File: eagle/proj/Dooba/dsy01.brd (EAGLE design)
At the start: 100 x 80 mm, 73 parts, among them U1 STM32F071LQFP100, U10 S25FLXXXSSOIC16, U2 AS6C1608TSOPII-44, U3 STM32F030LQFP32, U4 STM32F030LQFP32, U5 STM32F030LQFP32, U6 STM32F030LQFP32, U7 STM32F030LQFP32, U8 MIC550XSOT23, U9 STM32F030LQFP32, X1 8MHz, X2 8MHz, X3 8MHz, X4 8MHz, X5 8MHz, X6 8MHz, X7 8MHz

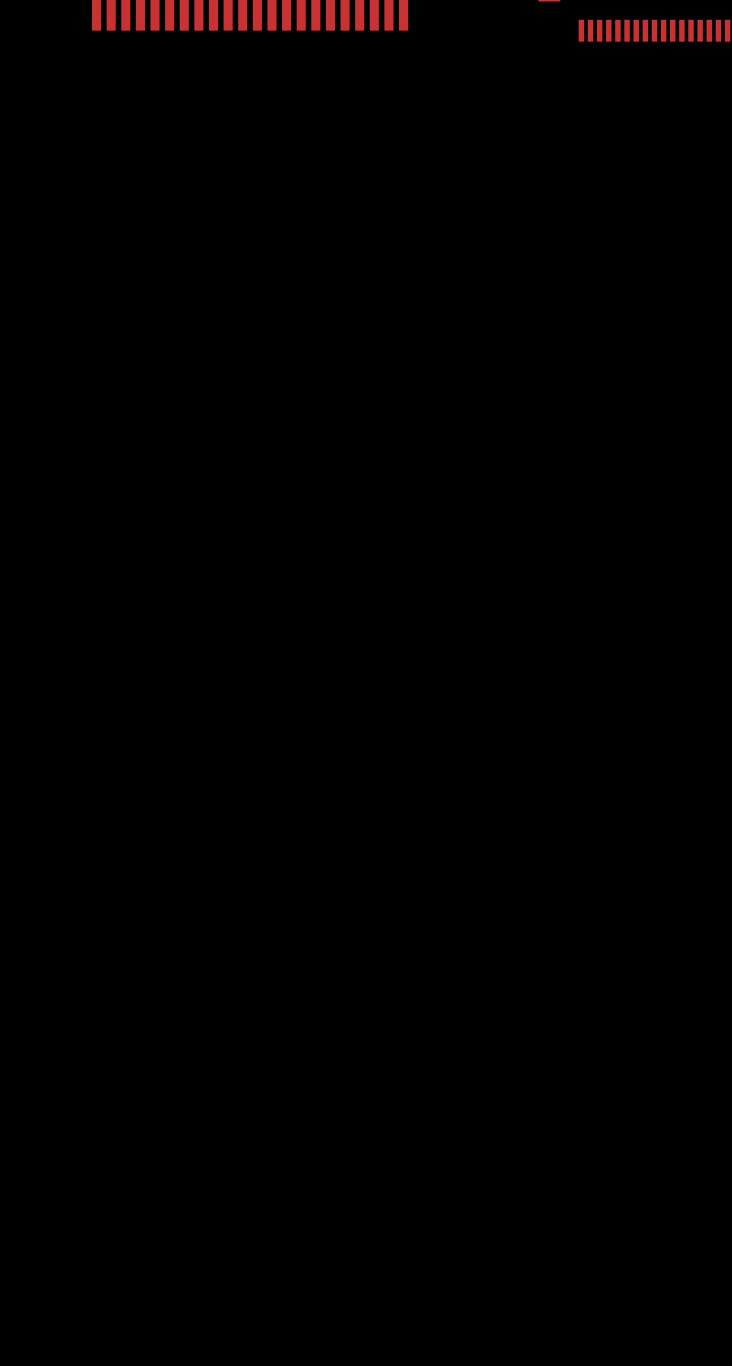
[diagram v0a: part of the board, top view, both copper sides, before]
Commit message: Added more Pin headers to Dooba Eagle Lib Added RST signal and extension header to DSY01
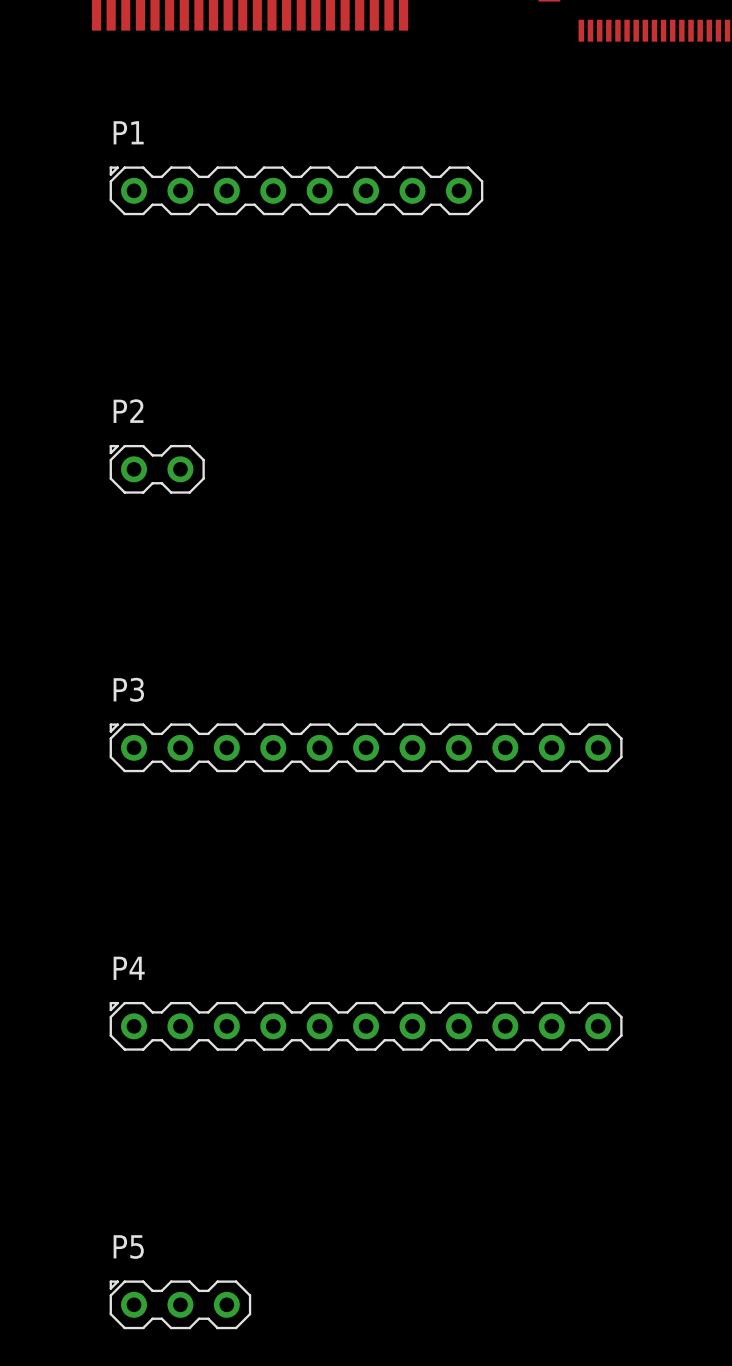
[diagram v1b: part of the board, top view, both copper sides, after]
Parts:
- added P1: DIO, dooba:PIN_8
- added P2: CKI-CKO, dooba:PIN_2
- added P3: NOT, dooba:PIN_11
- added P4: RDY, dooba:PIN_11
- added P5: PWR(VIN-GND-RST), dooba:PIN_3
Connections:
- new net N$35: P5.3, U1.14, U3.4, U5.4, U6.4, U7.4, U9.4
- new net N$36: U1.1, U2.41
- new net N$37: U1.2, U2.17
- new net N$38: U1.3, U2.40
- new net N$39: U1.4, U2.6
- net GND: now also P5.2
- net N$34: now also P5.1
- net N$55: now also P1.2
- net N$57: now also P3.5
- net N$58: now also P3.4
- net N$59: now also P3.3
- net N$60: now also P3.2
- net N$61: now also P3.1
- net N$63: now also P1.3
- net N$64: now also P3.6
- net N$65: now also P3.7
- net N$66: now also P3.8
- net N$67: now also P3.9
- net N$68: now also P3.10
- net N$69: now also P3.11
- net N$71: now also P1.4
- net N$72: now also P1.5
- net N$73: now also P1.6
- net N$75: now also P4.1
- net N$76: now also P4.2
- net N$77: now also P4.3
- net N$78: now also P4.4
- net N$79: now also P4.5
- net N$80: now also P4.8
- net N$81: now also P4.7
- net N$82: now also P4.6
- net N$83: now also P4.9
- net N$84: now also P4.10
- net N$85: now also P4.11
- net N$93: now also P1.7
- net N$94: now also P1.8
- net N$95: now also P2.2
- net N$96: now also P2.1
- net N$97: now also P1.1

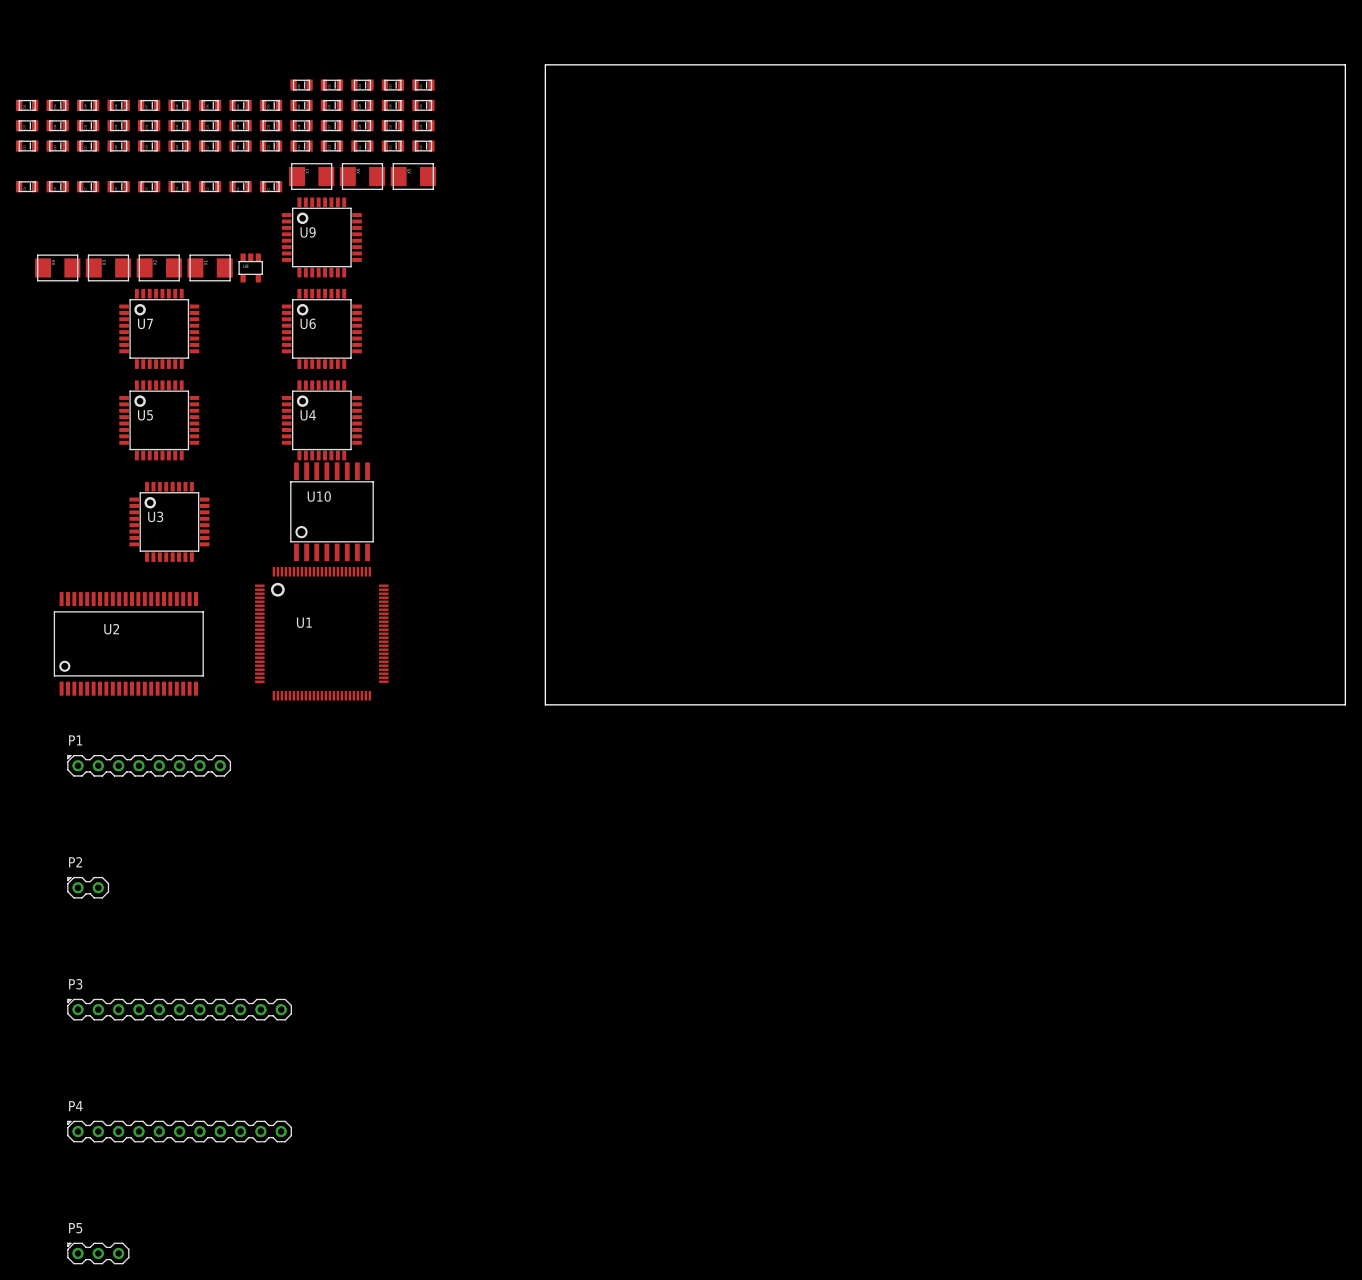
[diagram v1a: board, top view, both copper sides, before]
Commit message: Added CAM and DRU files for Eagle Further routed DSY01 board
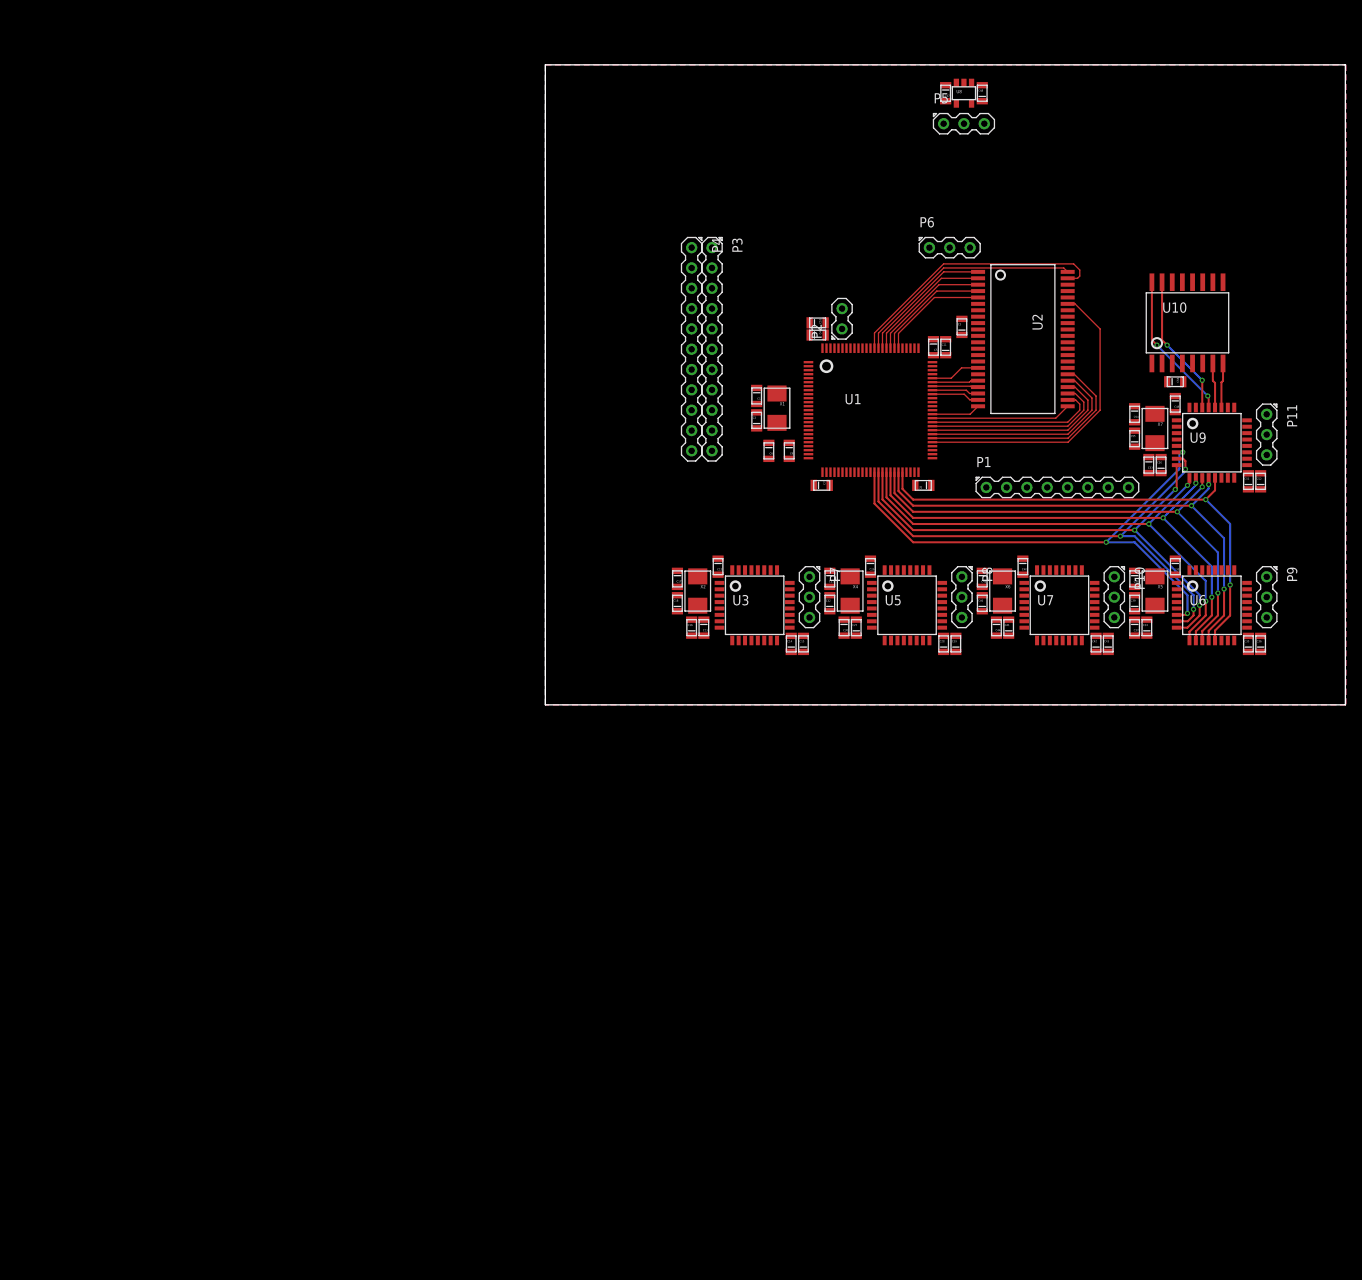
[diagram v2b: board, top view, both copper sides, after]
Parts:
- removed C19, C21: 100nF, dooba:0805
- removed C20: 10nF, dooba:0805
- removed C22: 4.7uF, dooba:0805
- removed C23: 1uF, dooba:0805
- removed C24, C25: 27pF, dooba:0805
- removed U4: STM32F030LQFP32, dooba:QFP32
- removed X3: 8MHz, dooba:XTAL_532
- added P10, P11, P6, P7, P8, P9: SWD_CORE(SWCLK-SWDIO-GND), dooba:PIN_3
- moved P5 177.9 mm to (52.3, 72.6)
- moved C36 163.7 mm to (89.4, 7.62), turned to 270 degrees
- moved C51 159.7 mm to (87.9, 27.9), turned to 270 degrees
- moved C35 158.8 mm to (87.9, 7.62), turned to 270 degrees
- moved C37 152.0 mm to (73.7, 9.65), turned to 90 degrees
- moved C50 145.1 mm to (77.0, 30.0), turned to 270 degrees
- moved C34 143.0 mm to (75.2, 9.65), turned to 270 degrees
- moved C49 140.9 mm to (78.7, 37.6), turned to 90 degrees
- moved C33 139.6 mm to (78.7, 17.3), turned to 90 degrees
- moved C43 124.4 mm to (70.4, 7.62), turned to 270 degrees
- moved C42 120.0 mm to (68.8, 7.62), turned to 270 degrees
- moved P1 118.8 mm to (64.0, 27.2)
- moved U2 118.1 mm to (59.7, 45.7), turned to 270 degrees
- moved C46 118.1 mm to (54.6, 12.7), turned to 270 degrees
- moved P2 118.1 mm to (37.1, 48.3), turned to 90 degrees
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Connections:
- removed net N$56: U4.13
- removed net N$70: U4.19
- removed net N$87: U4.18
- removed net N$88: U4.20
- removed net N$89: U4.21
- new net N$40: P6.1, U1.76
- new net N$41: P6.2, U1.72
- new net N$42: P7.2, U3.23
- net GND: now also P10.3, P11.3, P6.3, P7.3, P8.3, P9.3, U1.94, U3.31, U5.31, U6.31, U7.31, U9.31; no longer C19.2, C20.2, C21.2, C22.2, C23.1, C24.1, C25.1, U4.16, U4.32
- net N$45: now also P10.1, U7.24; no longer C24.2, U4.2, X3.1
- net N$46: now also P8.2, U5.23; no longer C25.2, U4.3, X3.2
- net N$47: now also P9.1, U6.24; no longer U4.6
- net N$48: now also P9.2, U6.23; no longer U4.7
- net N$49: now also P8.1, U5.24; no longer U4.8
- net N$50: now also P10.2, U7.23; no longer U4.9
- net N$51: now also P7.1, U3.24; no longer U4.10
- net N$52: now also P11.2, U9.23; no longer U4.11
- net N$53: now also P11.1, U9.24; no longer U4.12
- net VCC: no longer C19.1, C20.1, C21.1, C22.1, C23.2, U4.1, U4.17, U4.5
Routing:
- net N$97: track 0.00 -> 67.7 mm, vias 0 -> 3
- net N$55: track 0.00 -> 66.8 mm, vias 0 -> 3
- net N$63: track 0.00 -> 64.4 mm, vias 0 -> 3
- net N$71: track 0.00 -> 63.5 mm, vias 0 -> 3
- net N$72: track 0.00 -> 63.5 mm, vias 0 -> 3
- net N$73: track 0.00 -> 63.5 mm, vias 0 -> 3
- net N$93: track 0.00 -> 63.4 mm, vias 0 -> 3
- net N$94: track 0.00 -> 63.4 mm, vias 0 -> 2
- net N$3: track 0.00 -> 38.1 mm
- net N$30: track 0.00 -> 33.8 mm
- net N$29: track 0.00 -> 29.1 mm
- net N$12: track 0.00 -> 28.3 mm
- net N$13: track 0.00 -> 26.6 mm
- net N$14: track 0.00 -> 24.9 mm
- net N$15: track 0.00 -> 23.2 mm
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- added copper zone on layer 1, net GND
- added copper zone on layer 16, net GND

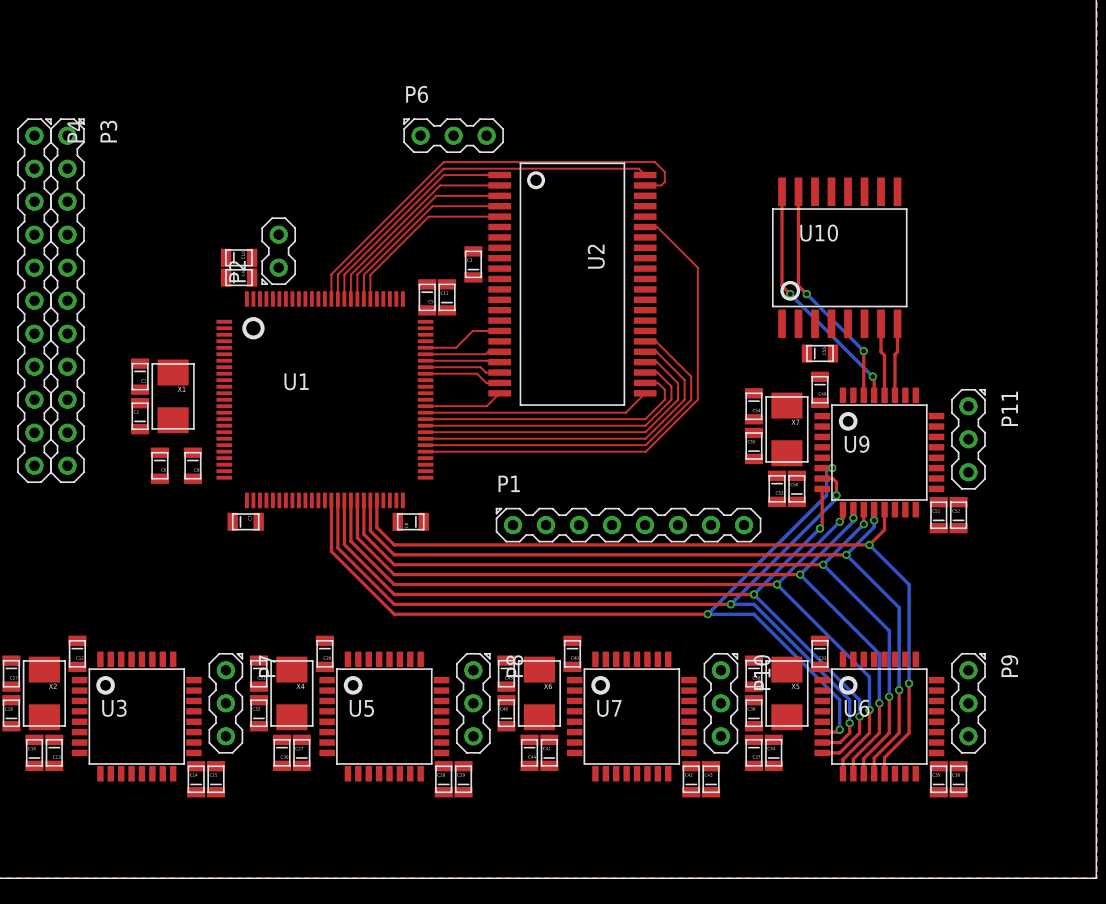
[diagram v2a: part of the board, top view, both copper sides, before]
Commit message: Further designed DSY01 Board & Schematic
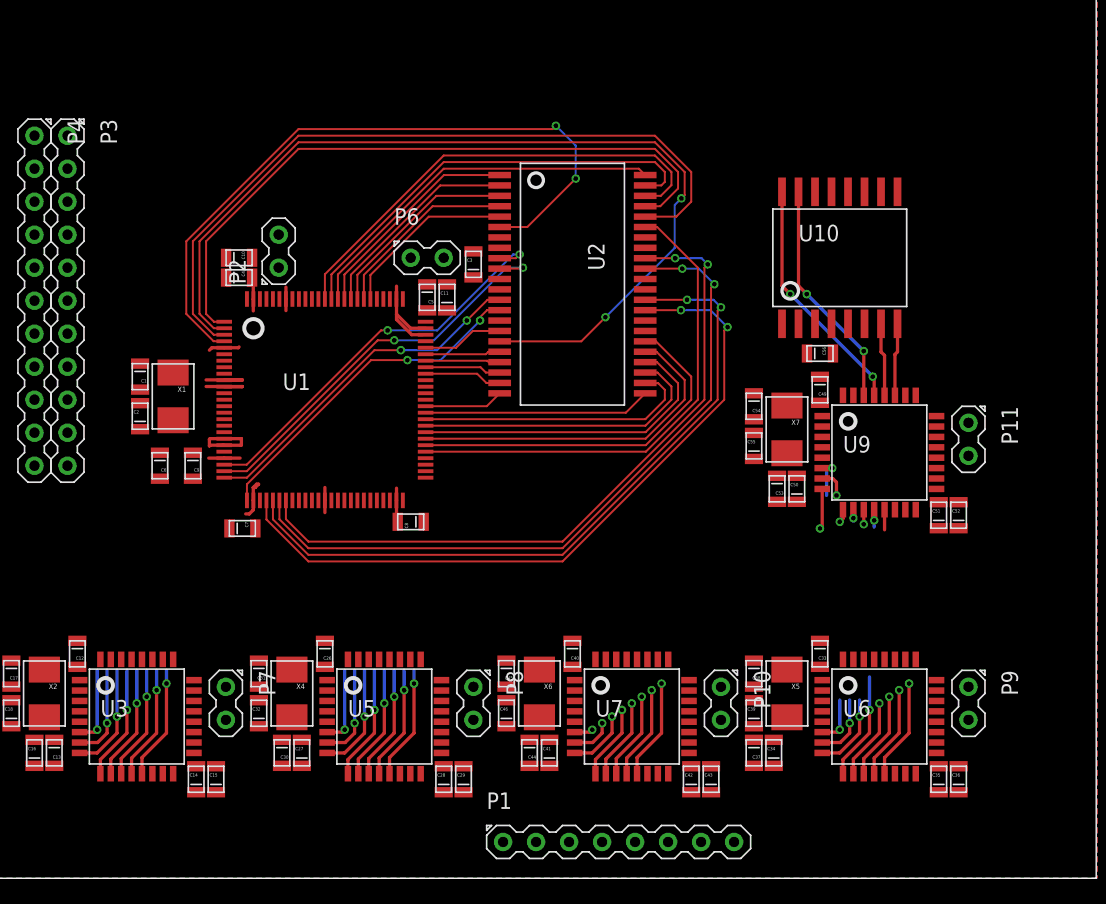
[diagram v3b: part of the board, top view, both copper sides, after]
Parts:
- P10, P11, P6, P7, P8, P9: device dooba:PIN_3 -> dooba:PIN_2
- moved P1 24.4 mm to (63.2, 2.79)
- moved P6 9.62 mm to (48.5, 47.8)
- moved C7 0.57 mm to (34.3, 26.9)
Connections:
- net GND: now also U1.10, U1.11, U1.19, U1.22, U1.38, U1.5, U1.73, U1.77, U3.14, U3.15, U3.22, U3.25, U3.26, U3.27, U3.28, U3.29, U3.30, U5.14, U5.15, U5.22, U5.25, U5.26, U5.27, U5.28, U5.29, U5.30, U6.14, U6.15, U6.22, U6.25, U6.26, U6.27, U6.28, U6.29, U6.30, U7.14, U7.15, U7.22, U7.25, U7.26, U7.27, U7.28, U7.29, U7.30, U9.14, U9.15, U9.22, U9.25, U9.26; no longer P10.3, P11.3, P6.3, P7.3, P8.3, P9.3
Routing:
- net N$37: track 0.00 -> 72.0 mm, vias 0 -> 2
- net N$38: track 0.00 -> 57.8 mm
- net N$7: track 0.00 -> 55.8 mm, vias 0 -> 2
- net N$5: track 0.00 -> 55.1 mm, vias 0 -> 2
- net N$6: track 0.00 -> 55.0 mm, vias 0 -> 2
- net N$4: track 0.00 -> 54.4 mm, vias 0 -> 2
- net N$39: track 0.00 -> 53.6 mm, vias 0 -> 2
- net N$36: track 0.00 -> 51.6 mm
- net N$97: track 67.7 -> 20.4 mm, vias 3 -> 5
- net N$55: track 66.8 -> 25.1 mm, vias 3 -> 5
- net GND: track 0.00 -> 39.0 mm
- net N$31: track 0.00 -> 36.3 mm
- net N$63: track 64.4 -> 30.6 mm, vias 3 -> 5
- net N$72: track 63.5 -> 31.0 mm, vias 3 -> 5
- net N$73: track 63.5 -> 32.1 mm, vias 3 -> 5
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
